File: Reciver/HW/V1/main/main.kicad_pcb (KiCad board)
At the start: 2 copper layers, 32.5 x 47.8 mm, 12 parts, among them U1 NodeMCU_1.0_(ESP-12E), U2 RFM95W-868S2

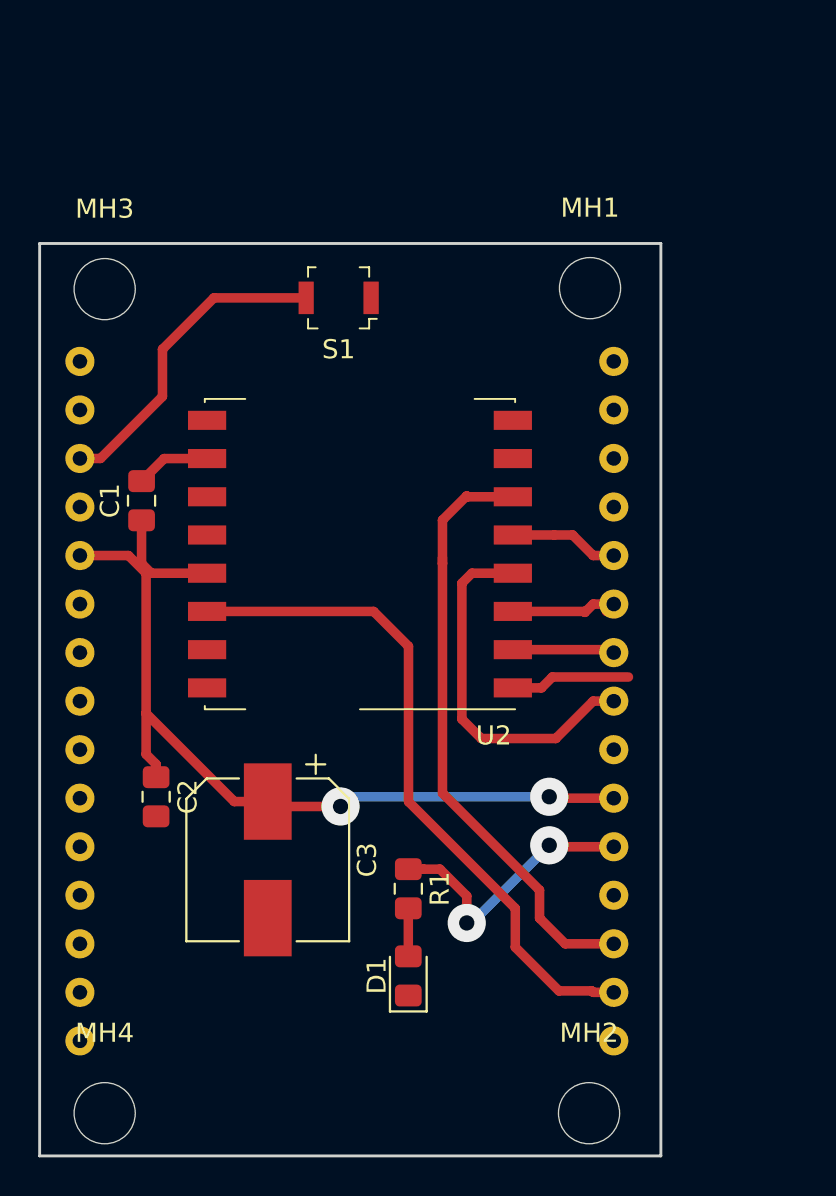
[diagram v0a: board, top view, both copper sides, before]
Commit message: Better foorprint
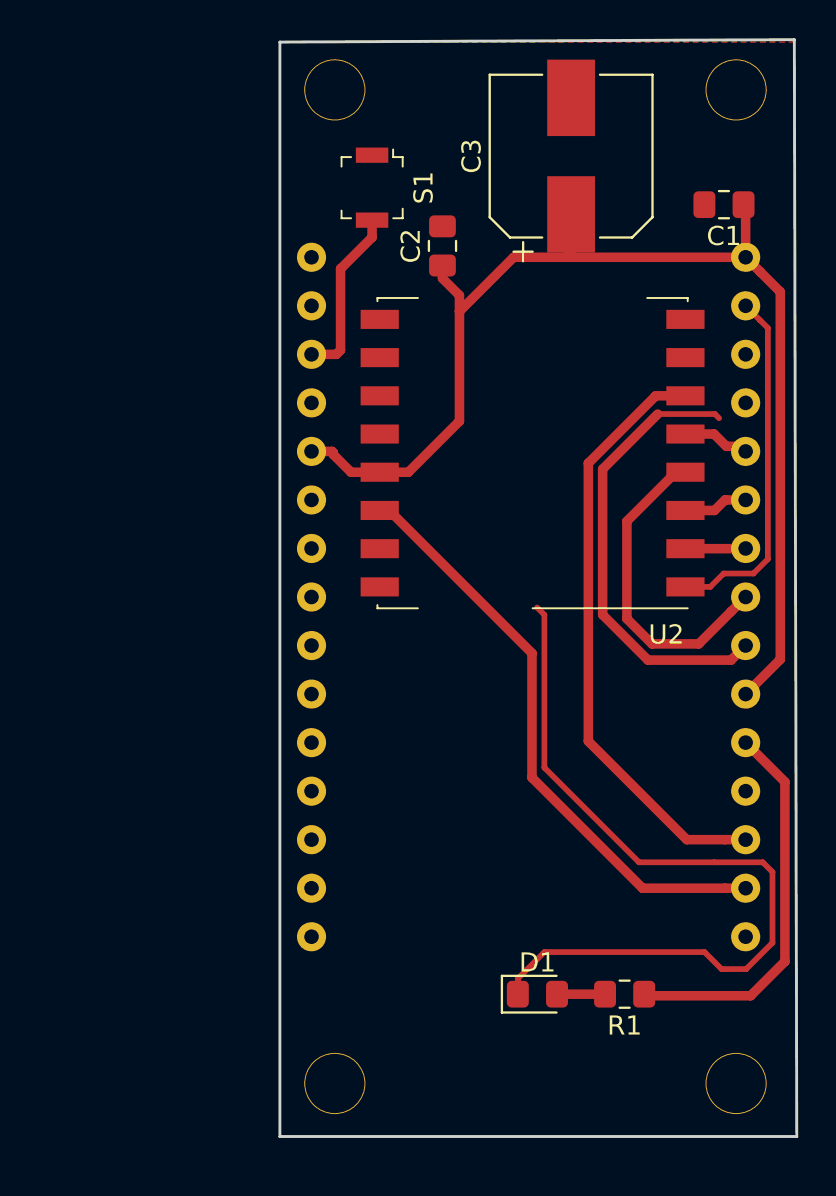
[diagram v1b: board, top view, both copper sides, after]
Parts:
- removed MH1, MH2, MH3, MH4: MountingHole, MountingHole:MountingHole_3.2mm_M3
- U1: footprint ESP8266:NodeMCU1.0(12-E) -> ESP8266:NodeMCU-LoLinV3
- moved C3 40.1 mm to (131.7, 55.4), turned to 90 degrees
- moved C1 34.2 mm to (139.7, 57.9), turned to 180 degrees
- moved C2 32.5 mm to (125.0, 60.1), turned to 90 degrees
- moved U1 22.7 mm to (116.8, 106.4)
- moved R1 12.6 mm to (134.5, 99.2), turned to 180 degrees
- moved U2 10.5 mm to (129.7, 70.9)
- moved D1 6.83 mm to (129.9, 99.2), turned to 0 degrees
- moved S1 6.03 mm to (121.3, 57.0), turned to 270 degrees
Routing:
- net GND: track 10.2 -> 84.5 mm
- net VCC: track 47.6 -> 63.5 mm, vias 2 -> 0
- net Net-(S1-Pad2): track 16.8 -> 9.10 mm
- net Net-(R1-Pad1): track 14.5 -> 20.0 mm, vias 2 -> 0
- net INT: track 35.5 -> 31.2 mm
- net MOSI: track 6.03 -> 3.38 mm
- net CS: track 5.73 -> 3.53 mm
- net MISO: track 5.35 -> 3.16 mm
- net SCK: track 19.2 -> 17.0 mm
- net RESET: track 32.4 -> 31.5 mm
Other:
- board size 32.5 x 47.8 mm -> 27.1 x 57.4 mm
